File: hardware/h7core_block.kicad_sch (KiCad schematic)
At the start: 84 parts, among them J1 USB-C, J3 TC2030-NL SWD, SW1 RESET, SW2 BOOT0, U1 STM32H743VIT6, U2 TPS2116DRLR, U3 AP63203WU-7, U4 TLV75533PDBVR, U5 IS25LP064A, U6 PCM5102APWR, U8 PCM1808PWR, Y1 25MHz 12pF

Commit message: feat(hardware): refs RVGAIN/ENC101-103/SWBYPASS/SWBOOT/SWRESET, silk pass, control rows at 22.25 mm
Owner 2026-10-02: control rows y 165 (RV101-RV109) and y 130 (RV110-RV114,
RVGAIN, ENC101-103), 5 mm side padding, equal pitch. foreman silk applied;
one 1.0 mm designator on silk per pot/encoder/switch/jack, LCSC/MPN text
hidden. ERC 0, netlist parity 0/0/0.
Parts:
- removed SW1: RESET, cubevox_h7core:SW-SMD_4P-L5.1-W5.1-P3.70-LS6.5-TL_H1.5, symbol cubevox_h7core:TS-1187A-B-A-B
- removed SW2: BOOT0, cubevox_h7core:SW-SMD_4P-L5.1-W5.1-P3.70-LS6.5-TL_H1.5, symbol cubevox_h7core:TS-1187A-B-A-B
- added SWBOOT: BOOT0, cubevox_h7core:SW-SMD_4P-L5.1-W5.1-P3.70-LS6.5-TL_H1.5, symbol cubevox_h7core:TS-1187A-B-A-B
- added SWRESET: RESET, cubevox_h7core:SW-SMD_4P-L5.1-W5.1-P3.70-LS6.5-TL_H1.5, symbol cubevox_h7core:TS-1187A-B-A-B
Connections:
- net 3V3: now also SWBOOT.3 (C), SWBOOT.4 (D)
- net BOOT0: now also SWBOOT.1 (A), SWBOOT.2 (B)
- net GND: now also SWRESET.3 (C), SWRESET.4 (D)
- net NRST: now also SWRESET.1 (A), SWRESET.2 (B)
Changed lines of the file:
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@@
 		(on_board yes)
 		(dnp no)
-		(property "Reference" "SW1"
+		(property "Reference" "SWRESET"
 			(at 82.55 299.72 0)
 			(effects
@@
 			(project "cubevox"
 				(path "/99ad1494-2bf8-5051-8886-2c8b83c86254/cdf9c81d-d554-530c-ae51-0929232e7fb3"
-					(reference "SW1")
+					(reference "SWRESET")
 					(unit 1)
 				)
@@
 		(on_board yes)
 		(dnp no)
-		(property "Reference" "SW2"
+		(property "Reference" "SWBOOT"
 			(at 114.3 299.72 0)
 			(effects
@@
 			(project "cubevox"
 				(path "/99ad1494-2bf8-5051-8886-2c8b83c86254/cdf9c81d-d554-530c-ae51-0929232e7fb3"
-					(reference "SW2")
+					(reference "SWBOOT")
 					(unit 1)
 				)

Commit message: feat(hardware): SH1106 1.3in OLED module footprint + model; owner's panel layout; refs end in 1
Footprint OLED-1.3-SH1106-I2C-4P from the vendor drawings (35.4x33.5,
holes 30.4x28.5, 4-pin header GND/VCC/SCL/SDA, active area on User.1),
STEP on 8 mm standoffs. J117 pins now GND, 3V3, SCL, SDA. Panel: bypass
and gain under the jacks, OLED + menu encoder centred, eight stage
columns with KEY and SEMITONES in columns 1-2. RVGAIN1 / SWBYPASS1 /
SWBOOT1 / SWRESET1 clear KiCad's annotation warning. ERC 0, parity 0/0/0.
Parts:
- removed SWBOOT: BOOT0, cubevox_h7core:SW-SMD_4P-L5.1-W5.1-P3.70-LS6.5-TL_H1.5, symbol cubevox_h7core:TS-1187A-B-A-B
- removed SWRESET: RESET, cubevox_h7core:SW-SMD_4P-L5.1-W5.1-P3.70-LS6.5-TL_H1.5, symbol cubevox_h7core:TS-1187A-B-A-B
- added SWBOOT1: BOOT0, cubevox_h7core:SW-SMD_4P-L5.1-W5.1-P3.70-LS6.5-TL_H1.5, symbol cubevox_h7core:TS-1187A-B-A-B
- added SWRESET1: RESET, cubevox_h7core:SW-SMD_4P-L5.1-W5.1-P3.70-LS6.5-TL_H1.5, symbol cubevox_h7core:TS-1187A-B-A-B
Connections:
- net 3V3: now also SWBOOT1.3 (C), SWBOOT1.4 (D)
- net BOOT0: now also SWBOOT1.1 (A), SWBOOT1.2 (B)
- net GND: now also SWRESET1.3 (C), SWRESET1.4 (D)
- net NRST: now also SWRESET1.1 (A), SWRESET1.2 (B)
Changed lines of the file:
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@@
 		(on_board yes)
 		(dnp no)
-		(property "Reference" "SWRESET"
+		(property "Reference" "SWRESET1"
 			(at 82.55 299.72 0)
 			(effects
@@
 			(project "cubevox"
 				(path "/99ad1494-2bf8-5051-8886-2c8b83c86254/cdf9c81d-d554-530c-ae51-0929232e7fb3"
-					(reference "SWRESET")
+					(reference "SWRESET1")
 					(unit 1)
 				)
@@
 		(on_board yes)
 		(dnp no)
-		(property "Reference" "SWBOOT"
+		(property "Reference" "SWBOOT1"
 			(at 114.3 299.72 0)
 			(effects
@@
 			(project "cubevox"
 				(path "/99ad1494-2bf8-5051-8886-2c8b83c86254/cdf9c81d-d554-530c-ae51-0929232e7fb3"
-					(reference "SWBOOT")
+					(reference "SWBOOT1")
 					(unit 1)
 				)

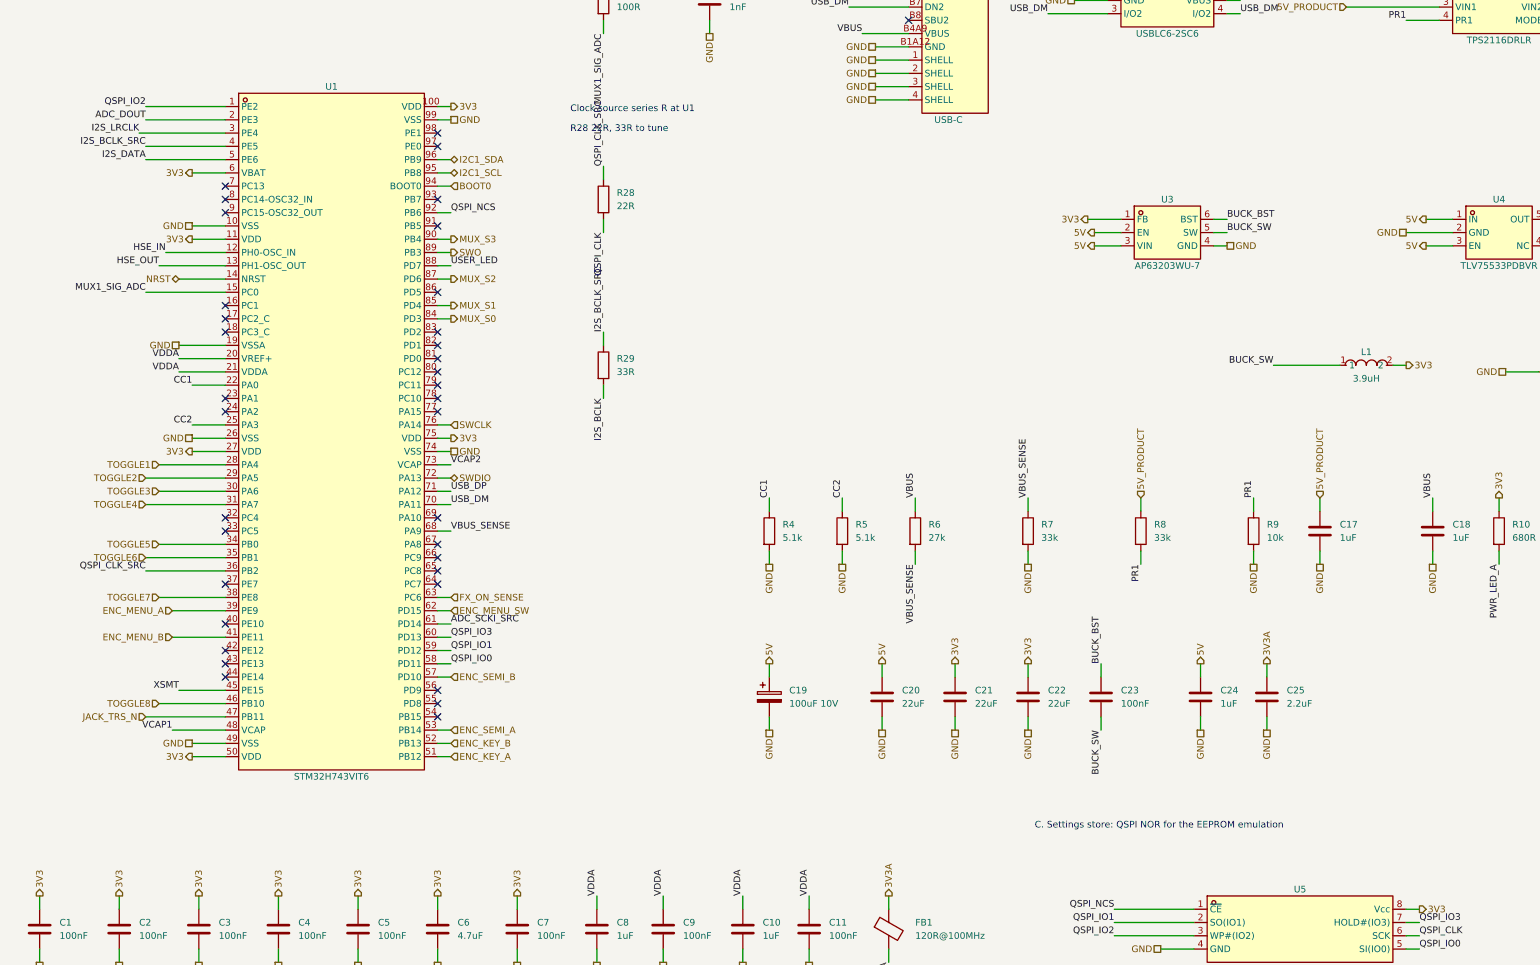
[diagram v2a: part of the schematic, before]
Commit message: feat(hardware): revision 2 analog chain in schematic, board and parts
Implements the accepted audit findings: OPA2197 preamp with AC-coupled
gain legs (DC gain 1), 0.1 % difference amp, isolated VREF follower
(22 R + 10 uF), pot-as-feedback stage 2 over 200 R + 100 uF, DAC and
output coupling as electrolytics, both NCJ6FA-H T pads tied (no sense
GPIO), ADC SCKI from SAI1_MCLK_A on PE2 with QSPI moved to bank 2.
ERC 0, netlist parity 0/0/0, owner-placed panel parts unmoved. Adds
the audit, its response, and the evidence capture.
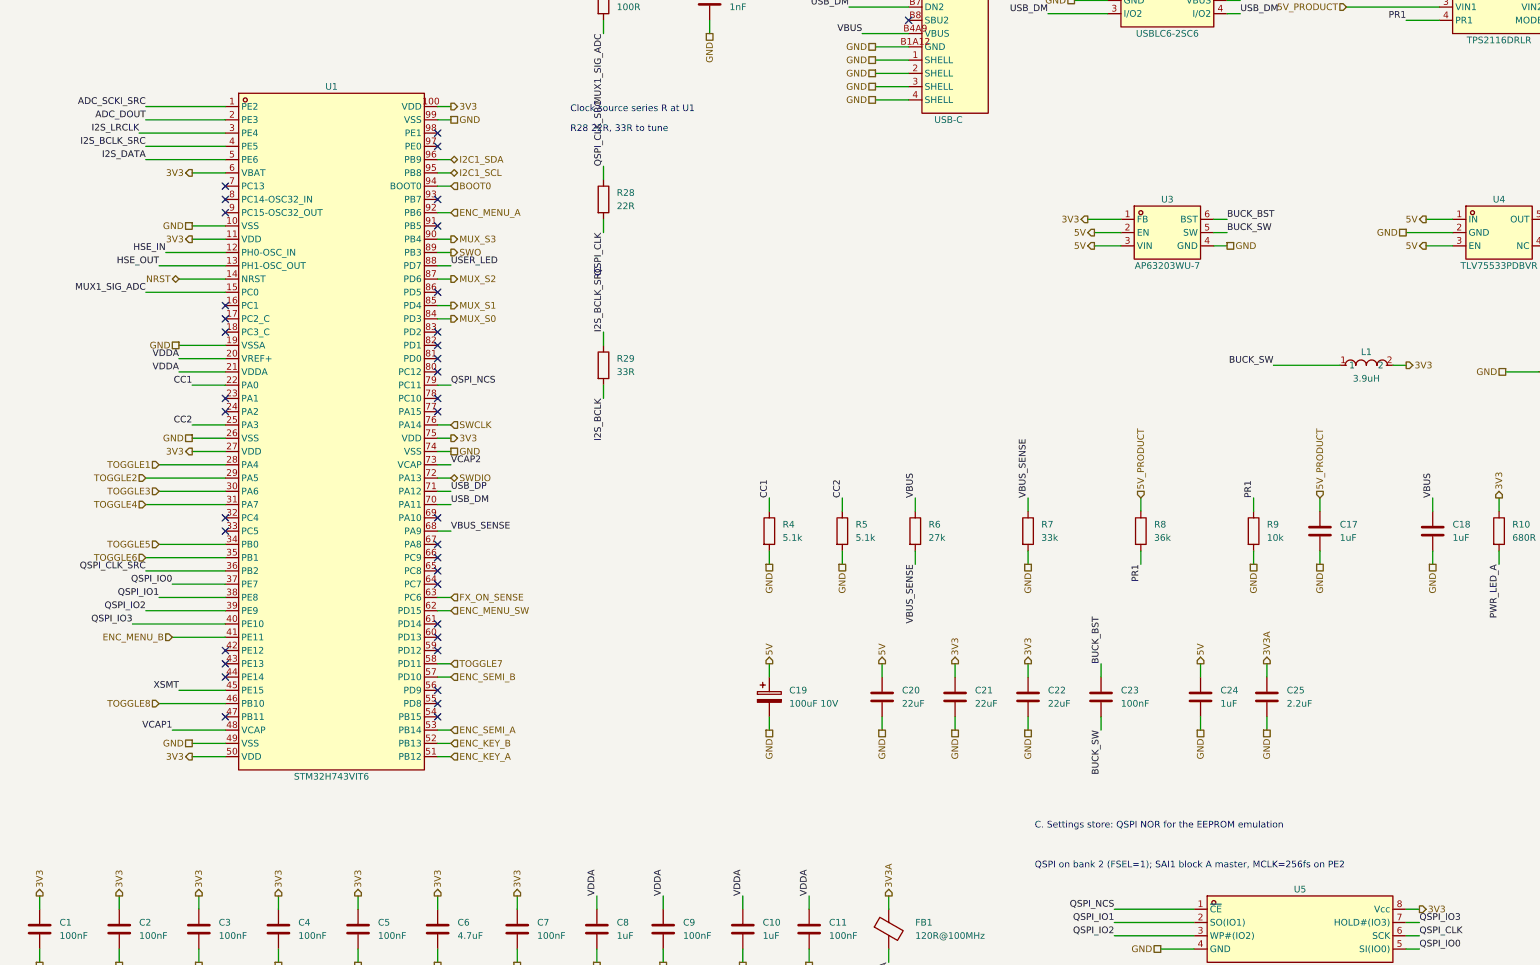
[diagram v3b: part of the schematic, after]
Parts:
- R8: value 33k -> 36k; LCSC C4216 -> C23147
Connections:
- net ADC_SCKI_SRC: now also U1.1 (PE2); no longer U1.61 (PD14)
- net ENC_MENU_A: now also U1.92 (PB6); no longer U1.39 (PE9)
- net QSPI_IO0: now also U1.37 (PE7); no longer U1.58 (PD11)
- net QSPI_IO1: now also U1.38 (PE8); no longer U1.59 (PD12)
- net QSPI_IO2: now also U1.39 (PE9); no longer U1.1 (PE2)
- net QSPI_IO3: now also U1.40 (PE10); no longer U1.60 (PD13)
- net QSPI_NCS: now also U1.79 (PC11); no longer U1.92 (PB6)
- net TOGGLE7: now also U1.58 (PD11); no longer U1.38 (PE8)
- net JACK_TRS_N: no longer names the net of U1.47 (PB11)
- no-connect marks 40 -> 41
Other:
- note added: "QSPI on bank 2 (FSEL=1); SAI1 block A master, MCLK=256fs on PE2"
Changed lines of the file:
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@@
 		)
 	)
-	(label "QSPI_IO2"
+	(label "ADC_SCKI_SRC"
 		(at 39.37 77.47 180)
 		(fields_autoplaced yes)
@@
 		)
 	)
-	(no_connect
-		(at 54.61 168.91)
+	(wire
+		(pts
+			(xy 54.61 168.91) (xy 44.45 168.91)
+		)
+		(stroke
+			(width 0)
+			(type default)
+		)
+	)
+	(label "QSPI_IO0"
+		(at 44.45 168.91 180)
+		(fields_autoplaced yes)
+		(effects
+			(font
+				(size 1.27 1.27)
+			)
+			(justify right bottom)
+		)
 	)
 	(wire
@@
 		)
 	)
-	(hierarchical_label "TOGGLE7"
-		(shape input)
+	(label "QSPI_IO1"
 		(at 41.91 171.45 180)
 		(fields_autoplaced yes)
@@
 	(wire
 		(pts
-			(xy 54.61 173.99) (xy 44.45 173.99)
+			(xy 54.61 173.99) (xy 39.37 173.99)
 		)
 		(stroke
@@
 		)
 	)
-	(hierarchical_label "ENC_MENU_A"
-		(shape input)
-		(at 44.45 173.99 180)
+	(label "QSPI_IO2"
+		(at 39.37 173.99 180)
 		(fields_autoplaced yes)
 		(effects
@@
 		)
 	)
-	(no_connect
-		(at 54.61 176.53)
+	(wire
+		(pts
+			(xy 54.61 176.53) (xy 36.83 176.53)
+		)
+		(stroke
+			(width 0)
+			(type default)
+		)
+	)
+	(label "QSPI_IO3"
+		(at 36.83 176.53 180)
+		(fields_autoplaced yes)
+		(effects
+			(font
+				(size 1.27 1.27)
+			)
+			(justify right bottom)
+		)
 	)
 	(wire
@@
 		)
 	)
-	(wire
-		(pts
-			(xy 54.61 194.31) (xy 39.37 194.31)
-		)
-		(stroke
-			(width 0)
-			(type default)
-		)
-	)
-	(hierarchical_label "JACK_TRS_N"
-		(shape input)
-		(at 39.37 194.31 180)
-		(fields_autoplaced yes)
-		(effects
-			(font
-				(size 1.27 1.27)
-			)
-			(justify right bottom)
-		)
+	(no_connect
+		(at 54.61 194.31)
 	)
 	(wire
@@
 		)
 	)
-	(label "QSPI_IO0"
+	(hierarchical_label "TOGGLE7"
+		(shape input)
 		(at 97.79 184.15 0)
 		(fields_autoplaced yes)
@@
 		)
 	)
-	(wire
-		(pts
-			(xy 95.25 181.61) (xy 97.79 181.61)
-		)
-		(stroke
-			(width 0)
-			(type default)
-		)
-	)
-	(label "QSPI_IO1"
-		(at 97.79 181.61 0)
-		(fields_autoplaced yes)
-		(effects
-			(font
-				(size 1.27 1.27)
-			)
-			(justify left bottom)
-		)
-	)
-	(wire
-		(pts
-			(xy 95.25 179.07) (xy 97.79 179.07)
-		)
-		(stroke
-			(width 0)
-			(type default)
-		)
-	)
-	(label "QSPI_IO3"
-		(at 97.79 179.07 0)
-		(fields_autoplaced yes)
-		(effects
-			(font
-				(size 1.27 1.27)
-			)
-			(justify left bottom)
-		)
+	(no_connect
+		(at 95.25 181.61)
 	)
-	(wire
-		(pts
-			(xy 95.25 176.53) (xy 97.79 176.53)
-		)
-		(stroke
-			(width 0)
-			(type default)
-		)
+	(no_connect
+		(at 95.25 179.07)
 	)
-	(label "ADC_SCKI_SRC"
-		(at 97.79 176.53 0)
-		(fields_autoplaced yes)
-		(effects
-			(font
-				(size 1.27 1.27)
-			)
-			(justify left bottom)
-		)
+	(no_connect
+		(at 95.25 176.53)
 	)
 	(wire
@@
 		(at 95.25 133.35)
 	)
-	(no_connect
-		(at 95.25 130.81)
+	(wire
+		(pts
+			(xy 95.25 130.81) (xy 97.79 130.81)
+		)
+		(stroke
+			(width 0)
+			(type default)
+		)
+	)
+	(label "QSPI_NCS"
+		(at 97.79 130.81 0)
+		(fields_autoplaced yes)
+		(effects
+			(font
+				(size 1.27 1.27)
+			)
+			(justify left bottom)
+		)
 	)
 	(no_connect
@@
 		)
 	)
-	(label "QSPI_NCS"
+	(hierarchical_label "ENC_MENU_A"
+		(shape input)
 		(at 97.79 97.79 0)
 		(fields_autoplaced yes)
@@
 			)
 		)
-		(property "Value" "33k"
+		(property "Value" "36k"
 			(at 232.41 160.02 0)
 			(effects
@@
 			)
 		)
-		(property "LCSC" "C4216"
+		(property "LCSC" "C23147"
 			(at 229.87 158.75 0)
 			(hide yes)
@@
 		(effects
 			(font
+				(size 1.27 1.27)
+			)
+			(justify left bottom)
+		)
+	)
+	(text "QSPI on bank 2 (FSEL=1); SAI1 block A master, MCLK=256fs on PE2"
+		(at 209.55 223.52 0)
+		(effects
+			(font

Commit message: feat(hardware): revision 3 analog chain, 9 V only, no external flash
Removes the QSPI flash, the TPS2116 USB power mux and the duplicate M2
OLED holes. Settings live in internal flash bank 2; USB is data only.
Codex round 2 (hardware/audit) accepted: stage 1 20 dB, TRS pad -25.7 dB,
47 uF mic coupling, bipolar C158, R116 330 R, relay pole B as the
FX_ON_SENSE dry contact, VBUS divider 33k/82k on PA9, output mute relay
K102 on PD12 with 5VA sense on PC4. ERC 0, netlist parity 0/0/0, panel
parts unmoved.
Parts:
- removed C17: 1uF, Capacitor_SMD:C_0603_1608Metric, symbol Device:C
- removed C26: 100nF, Capacitor_SMD:C_0603_1608Metric, symbol Device:C
- removed C60: 10nF, Capacitor_SMD:C_0402_1005Metric, symbol Device:C
- removed R11, R13, R9: 10k, Resistor_SMD:R_0402_1005Metric, symbol Device:R
- removed R12: 10k, Resistor_SMD:R_0603_1608Metric, symbol Device:R
- removed R28: 22R, Resistor_SMD:R_0603_1608Metric, symbol Device:R
- removed R8: 36k, Resistor_SMD:R_0603_1608Metric, symbol Device:R
- removed U2: TPS2116DRLR, cubevox_h7core:SOT-583-8_L2.1-W1.6-P0.50-LS1.6-BL, symbol cubevox_h7core:TPS2116DRLR
- removed U5: IS25LP064A, cubevox_h7core:SOIC-8_L5.3-W5.3-P1.27-LS7.9-BL, symbol cubevox_h7core:IS25LP064A-JBLE-TR
- C18: LCSC C15849 -> C90540
- C59: Group stitch QSPI_IO1 hop, ADC_SCKI via A -> stitch ADC_SCKI via A
- R6: value 27k -> 33k; LCSC C22967 -> C4216
- R7: value 33k -> 82k; LCSC C4216 -> C23254
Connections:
- net VA_SENSE: now reaches U1.32 (PC4)
- net MUTE_N: now reaches U1.59 (PD12)
- net QSPI_CLK_SRC: no longer names the net of U1.36 (PB2)
- net QSPI_IO0: no longer names the net of U1.37 (PE7)
- net QSPI_IO1: no longer names the net of U1.38 (PE8)
- net QSPI_IO2: no longer names the net of U1.39 (PE9)
- net QSPI_IO3: no longer names the net of U1.40 (PE10)
- net QSPI_NCS: no longer names the net of U1.79 (PC11)
- no-connect marks 41 -> 44
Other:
- note added: "B. Power entry: USB-C data and ESD, 3V3 buck, 3V3A LDO, VBUS sense, power LED. 5V comes from the 9 V buck on the top sheet"
- note added: "C59 ADC_SCKI via A; C61 ADC_SCKI via B"
- note added: "SAI1 block A master, MCLK=256fs on PE2. Settings live in internal flash bank 2"
- note removed: "B. Power entry: USB-C, ESD, 5 V mux, 3V3 buck, 3V3A LDO, VBUS sense, power LED"
- note removed: "C. Settings store: QSPI NOR for the EEPROM emulation"
- note removed: "C59 QSPI_IO1 hop, ADC_SCKI via A; C60 QSPI_IO1, IO2, NCS hops, flash end; C61 ADC_SCKI via B"
- note removed: "QSPI on bank 2 (FSEL=1); SAI1 block A master, MCLK=256fs on PE2"
- note removed: "R28 22R, 33R to tune"
- moved on the sheet: C18

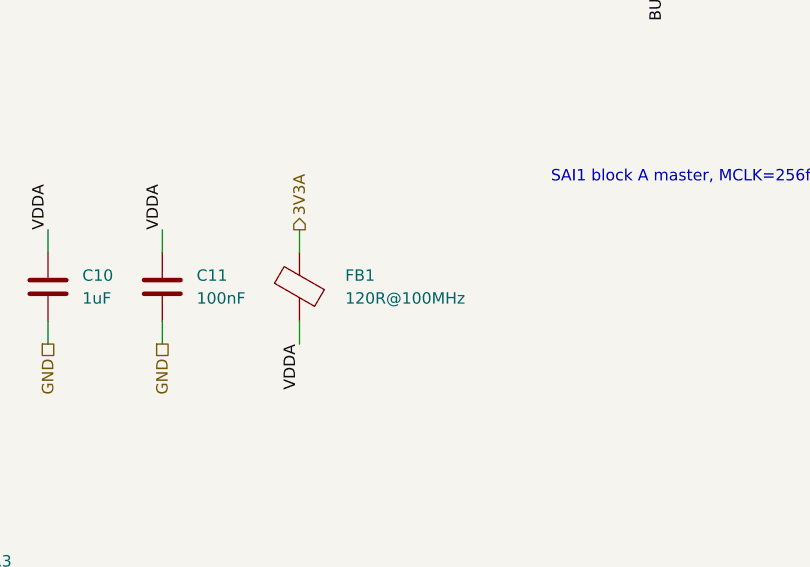
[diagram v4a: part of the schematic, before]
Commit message: feat(hardware): feed VDDA from VDD through FB1, add C164 10uF
AN4938 2.1.2: VDDA must stay within VDD + 0.3 V while VDD < 1 V. With FB1 fed from the separate 3V3A LDO nothing ordered the two rails. FB1 now takes 3V3, so VDDA follows VDD by construction. C164 (10 uF 0805, C15850) lowers the FB1 filter corner to ~60 kHz and damps its resonance. The generator also carries the J108 PJ-611E swap that was hand-edited into cubevox.json, so a regenerate no longer reverts it. Board: VDDA cluster rebuilt as a straight row FB1 > C8 > C164 > C10 with C9/C11 feeding C164; C55 moved beside R30; 32 mm 3V3A feed removed. ERC 0, DRC 0, D0175 ledger 0214.
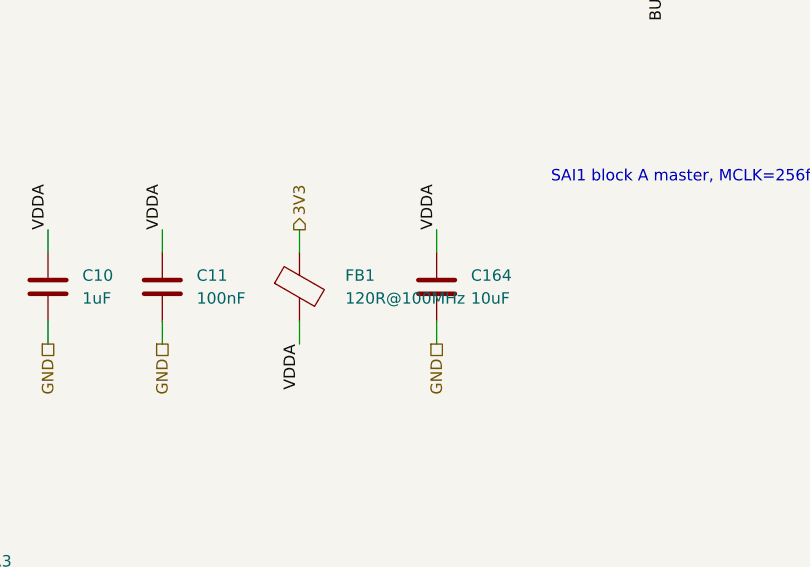
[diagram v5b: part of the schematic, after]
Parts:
- added C164: 10uF, Capacitor_SMD:C_0805_2012Metric, symbol Device:C
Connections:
- net 3V3: now also FB1.1
- net 3V3A: no longer FB1.1
- net GND: now also C164.2
- net VDDA: now also C164.1
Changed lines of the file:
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@@
 		)
 	)
-	(hierarchical_label "3V3A"
+	(hierarchical_label "3V3"
 		(shape output)
 		(at 181.61 228.6 90)
@@
 		(fields_autoplaced yes)
 		(effects
+			(font
+				(size 1.27 1.27)
+			)
+			(justify right bottom)
+		)
+	)
+	(symbol
+		(lib_id "Device:C")
+		(at 196.85 234.95 0)
+		(unit 1)
+		(exclude_from_sim no)
+		(in_bom yes)
+		(on_board yes)
+		(dnp no)
+		(property "Reference" "C164"
+			(at 200.66 233.68 0)
+			(effects
+				(font
+					(size 1.27 1.27)
+				)
+				(justify left)
+			)
+		)
+		(property "Value" "10uF"
+			(at 200.66 236.22 0)
+			(effects
+				(font
+					(size 1.27 1.27)
+				)
+				(justify left)
+			)
+		)
+		(property "Footprint" "Capacitor_SMD:C_0805_2012Metric"
+			(at 196.85 234.95 0)
+			(hide yes)
+			(effects
+				(font
+					(size 1.27 1.27)
+				)
+			)
+		)
+		(property "Datasheet" "~"
+			(at 196.85 234.95 0)
+			(hide yes)
+			(effects
+				(font
+					(size 1.27 1.27)
+				)
+			)
+		)
+		(property "LCSC" "C15850"
+			(at 196.85 234.95 0)
+			(hide yes)
+			(effects
+				(font
+					(size 1.27 1.27)
+				)
+			)
+		)
+		(pin "1"
+		)
+		(pin "2"
+		)
+		(instances
+			(project "cubevox"
+				(path "/99ad1494-2bf8-5051-8886-2c8b83c86254/cdf9c81d-d554-530c-ae51-0929232e7fb3"
+					(reference "C164")
+					(unit 1)
+				)
+			)
+		)
+	)
+	(wire
+		(pts
+			(xy 196.85 231.14) (xy 196.85 228.6)
+		)
+		(stroke
+			(width 0)
+			(type default)
+		)
+	)
+	(label "VDDA"
+		(at 196.85 228.6 90)
+		(fields_autoplaced yes)
+		(effects
+			(font
+				(size 1.27 1.27)
+			)
+			(justify left bottom)
+		)
+	)
+	(wire
+		(pts
+			(xy 196.85 238.76) (xy 196.85 241.3)
+		)
+		(stroke
+			(width 0)
+			(type default)
+		)
+	)
+	(hierarchical_label "GND"
+		(shape passive)
+		(at 196.85 241.3 270)
+		(fields_autoplaced yes)
+		(effects
